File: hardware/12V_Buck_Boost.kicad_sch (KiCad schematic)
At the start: 0 parts

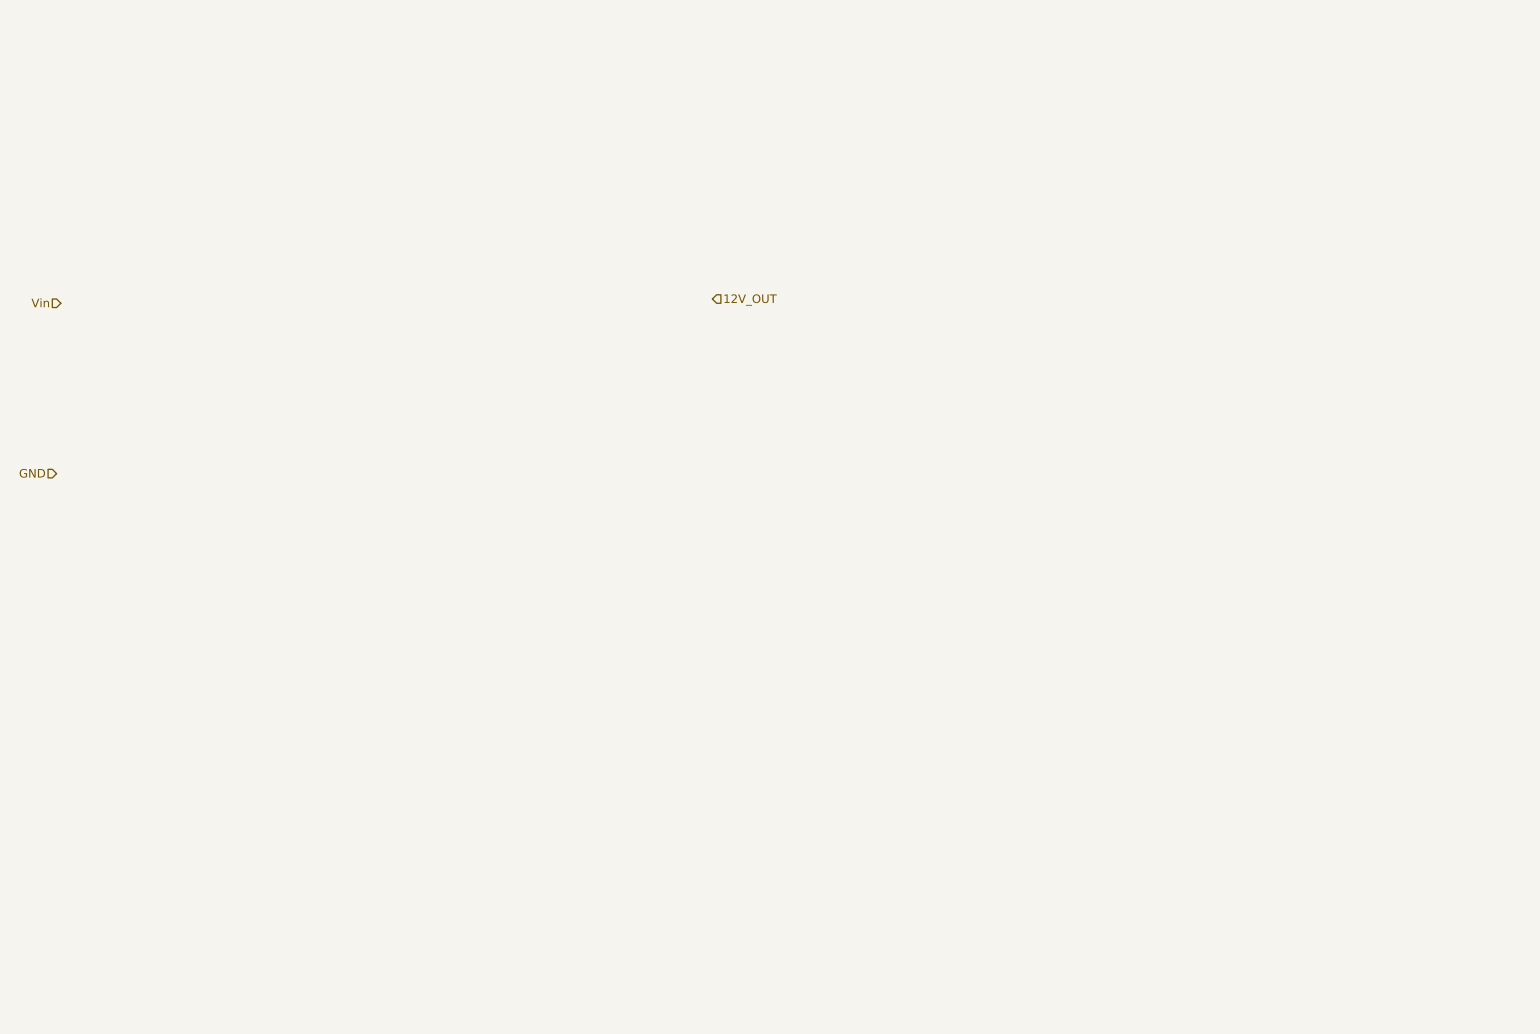
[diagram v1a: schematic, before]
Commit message: added 12V buck boost
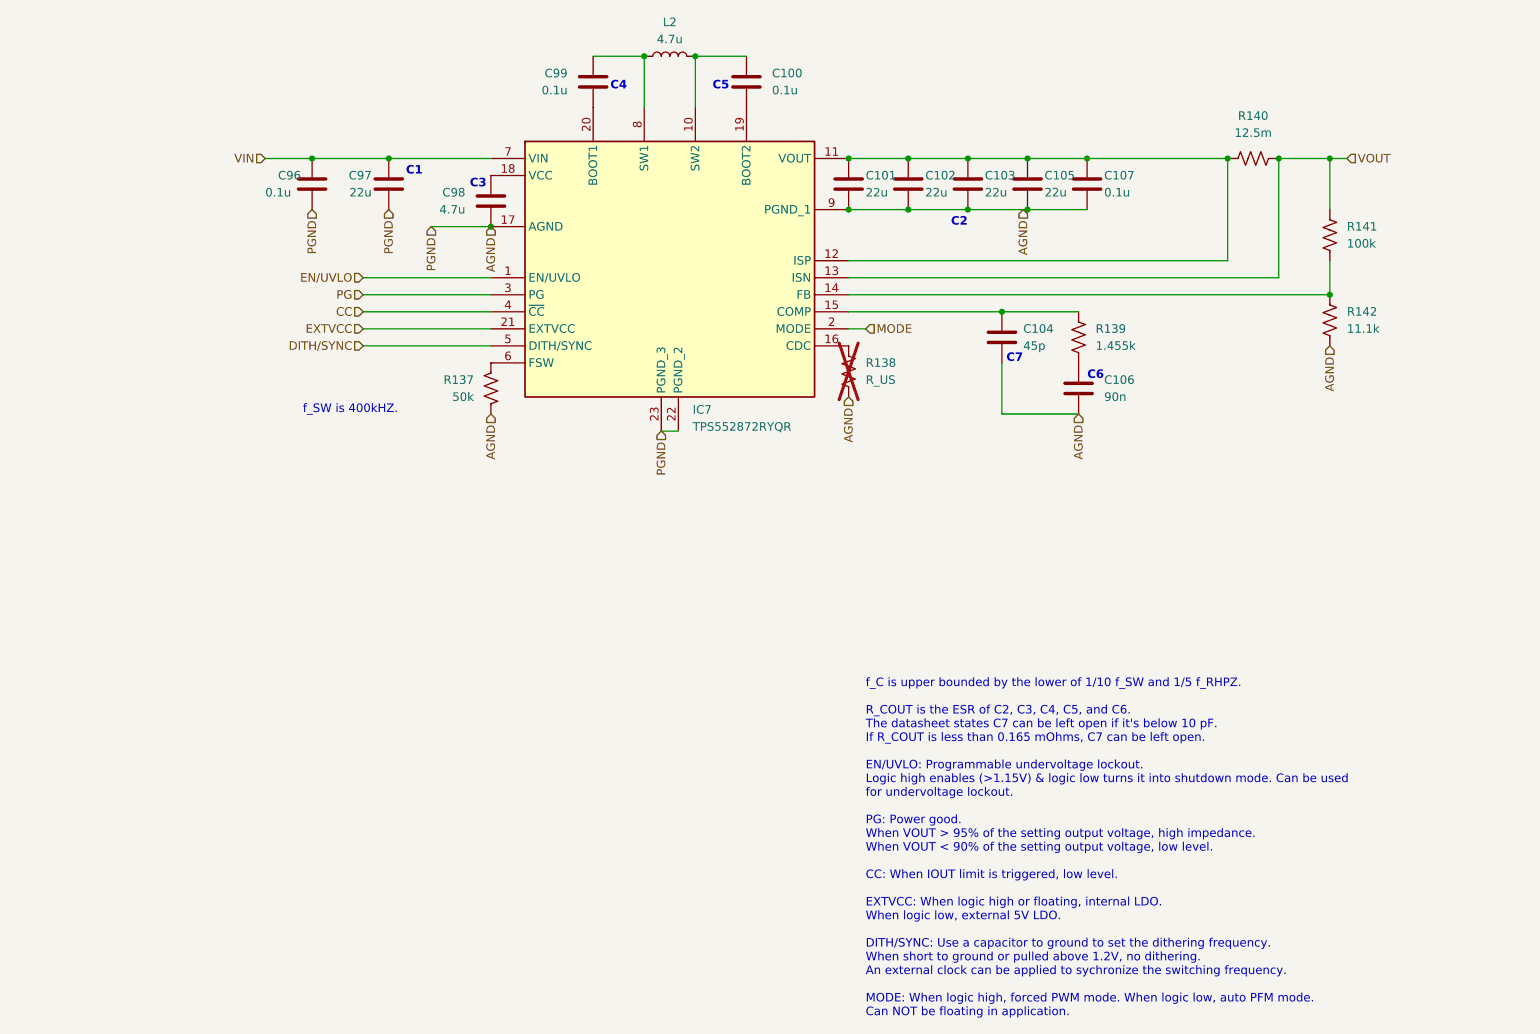
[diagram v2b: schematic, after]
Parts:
- added C100, C107, C96, C99: 0.1u, Capacitor_SMD:C_0603_1608Metric_Pad1.08x0.95mm_HandSolder, symbol Device:C
- added C101, C102, C103, C105, C97: 22u, Capacitor_SMD:C_1206_3216Metric, symbol Device:C
- added C104: 45p, Capacitor_SMD:C_0603_1608Metric_Pad1.08x0.95mm_HandSolder, symbol Device:C
- added C106: 90n, Capacitor_SMD:C_0603_1608Metric_Pad1.08x0.95mm_HandSolder, symbol Device:C
- added C98: 4.7u, Capacitor_SMD:C_0805_2012Metric_Pad1.18x1.45mm_HandSolder, symbol Device:C
- added IC7: TPS552872RYQR, LHRS_ICs:TPS552892QWRYQRQ1, symbol lhrs_ics:TPS552872RYQR
- added L2: 4.7u, LHRS_Passives:74439369082, symbol Device:L
- added R137: 50k, Resistor_SMD:R_0603_1608Metric_Pad0.98x0.95mm_HandSolder, symbol Device:R_US
- added R138: R_US, symbol Device:R_US
- added R139: 1.455k, Resistor_SMD:R_0603_1608Metric_Pad0.98x0.95mm_HandSolder, symbol Device:R_US
- added R140: 12.5m, Resistor_SMD:R_1210_3225Metric, symbol Device:R_US
- added R141: 100k, Resistor_SMD:R_0603_1608Metric_Pad0.98x0.95mm_HandSolder, symbol Device:R_US
- added R142: 11.1k, Resistor_SMD:R_0603_1608Metric_Pad0.98x0.95mm_HandSolder, symbol Device:R_US
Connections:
- new net: C99.2, IC7.8 (SW1), L2.1
- new net: C100.1, IC7.10 (SW2), L2.2
- new net: C101.1, C102.1, C103.1, C105.1, C107.1, IC7.11 (VOUT), IC7.12 (ISP), R140.1
- new net: IC7.14 (FB), R141.1, R142.1
- new net: C104.1, IC7.15 (COMP), R139.1
- new net: C106.1, R139.2
- new net: C99.1, IC7.20 (BOOT1)
- new net: IC7.16 (CDC), R138.2
- new net: C100.2, IC7.19 (BOOT2)
- new net: IC7.6 (FSW), R137.2
- new net: C98.1, IC7.18 (VCC)
- new net AGND: C101.2, C102.2, C103.2, C104.2, C105.2, C106.2, C107.2, C96.2, C97.2, C98.2, IC7.17 (AGND), IC7.22 (PGND_2), IC7.23 (PGND_3), IC7.9 (PGND_1), R137.1, R138.1, R142.2
- new net CC: IC7.4 (~{CC})
- new net DITH/SYNC: IC7.5 (DITH/SYNC)
- new net EN/UVLO: IC7.1 (EN/UVLO)
- new net EXTVCC: IC7.21 (EXTVCC)
- new net MODE: IC7.2 (MODE)
- new net PG: IC7.3 (PG)
- new net VIN: C96.1, C97.1, IC7.7 (VIN)
- new net VOUT: IC7.13 (ISN), R140.2, R141.2
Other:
- note added: "C1"
- note added: "C2"
- note added: "C3"
- note added: "C4"
- note added: "C5"
- note added: "C6"
- note added: "C7"
- note added: "f_C is upper bounded by the lower of 1/10 f_SW and 1/5 f_RHPZ. R_COUT is the ESR of C2, C3, C4, C5, and C6. The datasheet states C7 can be left open if it's below 10 pF. If R_COUT is less than 0.165 mOhms, C7 can be left open. EN/UVLO: Programmable undervoltage lockout. Logic high enables (>1.15V) & logic low turns it into shutdown mode. Can be used for undervoltage lockout. PG: Power good. When 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"
- note added: "f_SW is 400kHZ."

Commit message: review council
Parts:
- R138: footprint (none) -> Resistor_SMD:R_0603_1608Metric_Pad0.98x0.95mm_HandSolder; now in the parts list
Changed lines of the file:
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@@
 		(unit 1)
 		(body_style 1)
-		(exclude_from_sim yes)
-		(in_bom no)
-		(on_board no)
-		(in_pos_files no)
+		(exclude_from_sim no)
+		(in_bom yes)
+		(on_board yes)
+		(in_pos_files yes)
 		(dnp yes)
 		(fields_autoplaced yes)
@@
 			)
 		)
-		(property "Footprint" ""
+		(property "Footprint" "Resistor_SMD:R_0603_1608Metric_Pad0.98x0.95mm_HandSolder"
 			(at 173.609 68.961 90)
 			(hide yes)
